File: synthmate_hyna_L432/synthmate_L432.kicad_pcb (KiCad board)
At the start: 4 copper layers, 74 x 23 mm, 43 parts, among them J1 USB_C_synthmate, J3 USB_C_connector_board, J5 Conn_01x15, J7 Conn_01x04, J8 Conn_ST_STDC14, SW1 RotaryEncoder_Switch, SW2 SW_Push, SW3 SW_Push, U1 STM32L432KCUx, U2 TS3USB221ARSER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

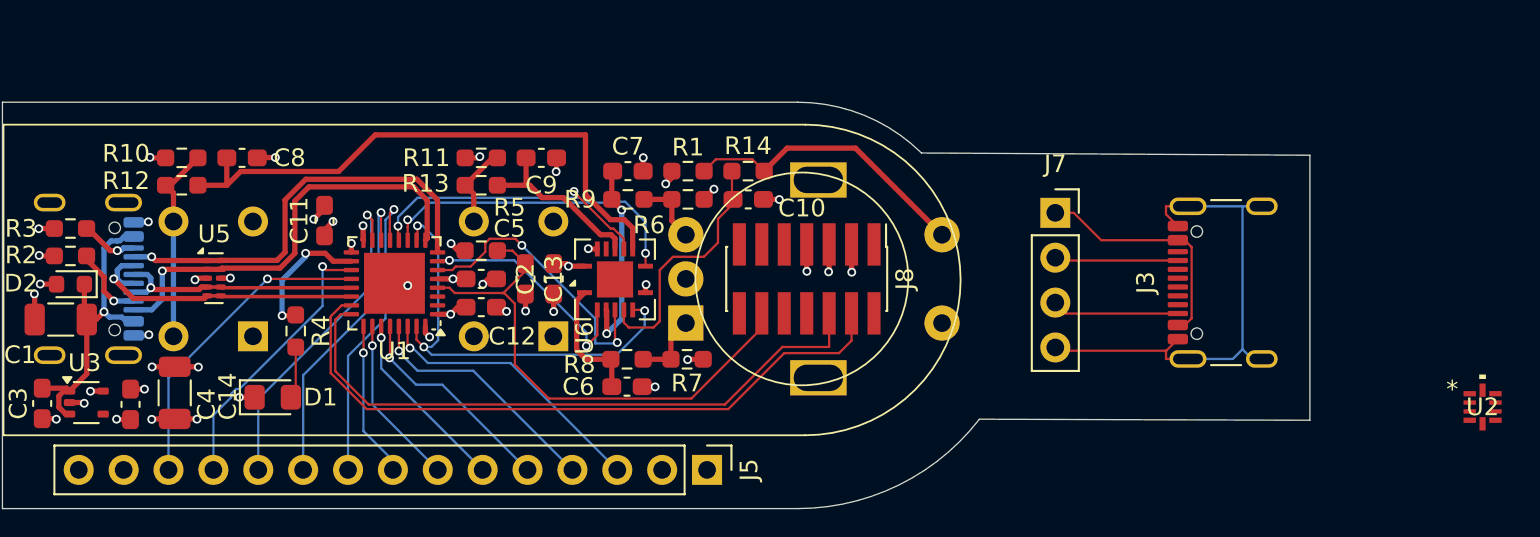
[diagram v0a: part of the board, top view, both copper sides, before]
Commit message: adapter board cleanup, uart IO protection added
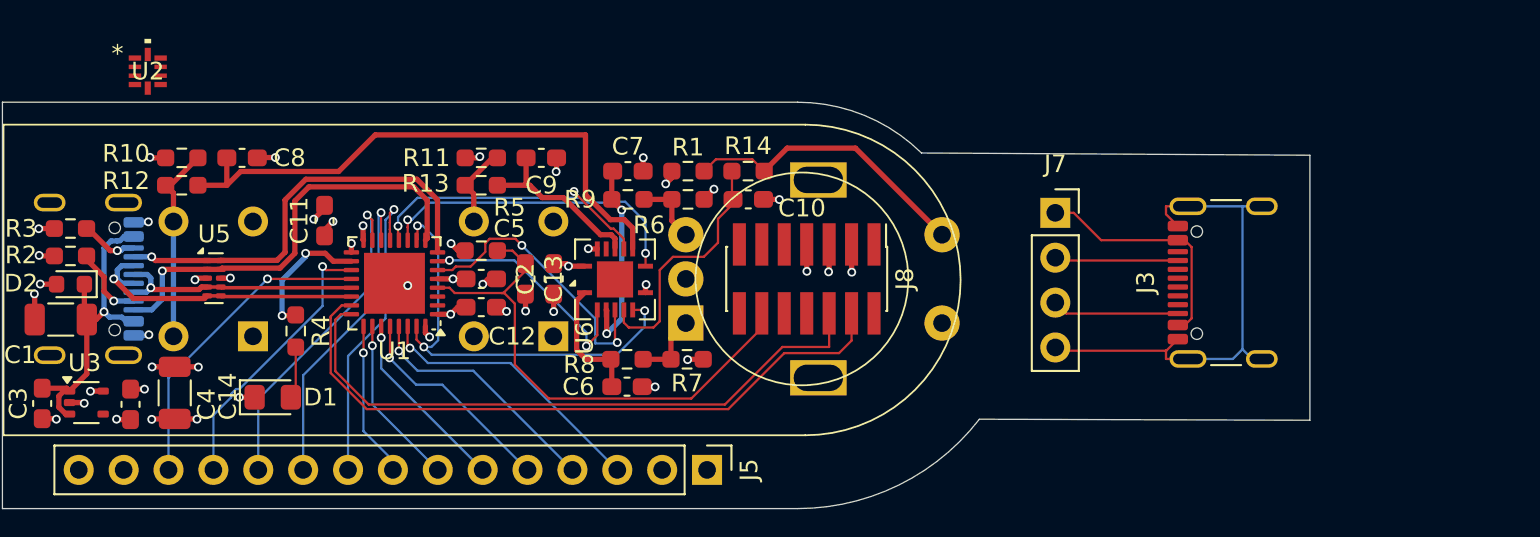
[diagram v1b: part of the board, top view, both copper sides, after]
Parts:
- moved U2 77.9 mm to (99.2, 35.2)
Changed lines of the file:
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@@
 	(footprint "footprints:RSE10"
 		(layer "F.Cu")
-		(at 174.7726 54.249999)
+		(at 99.2274 35.25)
 		(tags "TS3USB221ARSER ")
 		(property "Reference" "U2"

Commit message: V2_gerber
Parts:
- removed J3: USB_C_connector_board, Connector_USB:USB_C_Receptacle_GCT_USB4105-xx-A_16P_TopMnt_Horizontal
- removed J5: Conn_01x15, Connector_PinHeader_2.54mm:PinHeader_1x15_P2.54mm_Vertical
- removed J7: Conn_01x04, Connector_PinSocket_2.54mm:PinSocket_1x04_P2.54mm_Vertical
- removed U5: TPD4E02B04DQA, Package_SON:USON-10_2.5x1.0mm_P0.5mm
- added C15: 1uF, Capacitor_SMD:C_0603_1608Metric_Pad1.08x0.95mm_HandSolder, F.Cu at (104.0, 51.3)
- added C16: 1uF, Capacitor_SMD:C_0603_1608Metric_Pad1.08x0.95mm_HandSolder, F.Cu at (98.1, 40.7)
- added D3: D_Schottky, Diode_SMD:D_0603_1608Metric, F.Cu at (110.8, 42.0)
- added H1: MountingHole, MountingHole:MountingHole_2.1mm, F.Cu at (94.1, 39.3)
- added H2: MountingHole, MountingHole:MountingHole_2.1mm, F.Cu at (124.8, 53.5)
- added R16: 220R, Resistor_SMD:R_0603_1608Metric_Pad0.98x0.95mm_HandSolder, F.Cu at (104.5, 44.1)
- added R18: 20k, Resistor_SMD:R_0603_1608Metric_Pad0.98x0.95mm_HandSolder, F.Cu at (102.9, 53.7)
- added TP1: TestPoint, TestPoint:TestPoint_Pad_1.0x1.0mm, F.Cu at (107.0, 39.3)
- added TP2: TestPoint, TestPoint:TestPoint_Pad_1.0x1.0mm, F.Cu at (108.5, 54.9)
- added TP3: TestPoint, TestPoint:TestPoint_Pad_1.0x1.0mm, F.Cu at (110.6, 54.9)
- added TP4: TestPoint, TestPoint:TestPoint_Pad_1.0x1.0mm, F.Cu at (109.1, 39.3)
- added TP5: TestPoint, TestPoint:TestPoint_Pad_1.0x1.0mm, F.Cu at (123.5, 39.8)
- added TP6: TestPoint, TestPoint:TestPoint_Pad_1.0x1.0mm, F.Cu at (124.4, 49.6)
- added U4: SN74LV1T34DBV, Package_TO_SOT_SMD:SOT-23-5, F.Cu at (101.7, 43.7)
- C10, C11, C12, C2, C5, C6, C7, C8, C9: value 100nF -> 1uF
- J1: moved to F.Cu
- SW2, SW3: footprint Button_Switch_THT:SW_TH_Tactile_Omron_B3F-10xx -> Button_Switch_THT:Marquardt_6450
- moved U2 14.3 mm to (103.4, 49.0), turned to 180 degrees
- moved U6 10.6 mm to (117.1, 53.2), turned to 0 degrees
- moved C6 7.84 mm to (125.8, 45.3), turned to -90 degrees
- moved R8 6.34 mm to (127.3, 45.3), turned to -90 degrees
- moved SW2 5.45 mm to (100.8, 47.0), turned to 0 degrees
- moved SW3 5.43 mm to (117.8, 47.0), turned to 0 degrees
- moved C13 4.07 mm to (120.4, 50.6), turned to 90 degrees
- moved C2 3.89 mm to (122.0, 50.6), turned to 90 degrees
- moved R5 3.25 mm to (116.9, 42.4)
- moved R10 3.23 mm to (98.1, 39.1)
- moved C5 3.16 mm to (116.9, 44.1)
- moved C8 3.06 mm to (101.7, 39.1)
- moved R7 2.19 mm to (127.7, 50.9), turned to -90 degrees
- moved C9 1.54 mm to (120.3, 39.2)
- moved R11 1.54 mm to (116.9, 39.2)
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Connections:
- J1 pad A6: USB_DP -> /usb_P
- J1 pad A7: USB_DN -> /usb_N
- J1 pad A8: LPUART_TX -> unconnected-(J1-SBU1-PadA8)
- J1 pad B6: USB_DP -> /usb_P
- J1 pad B7: USB_DN -> /usb_N
- J1 pad B8: LPUART_RX -> unconnected-(J1-SBU2-PadB8)
- SW3 pad 1: GND -> Net-(R11-Pad1)
- SW3 pad 2: Net-(R11-Pad1) -> GND
- U1 pad 13: PA7 -> usb_switch
- U1 pad 19: USART1_TX -> Net-(U1-PA9)
- U1 pad 21: USB_DN -> /usb_mcu_N
- U1 pad 22: USB_DP -> /usb_mcu_P
- U1 pad 25: PA15 -> Net-(U1-PA15)
- U2 pad 1: unconnected-(U2-1D+-Pad1) -> USART1_TX
- U2 pad 10: unconnected-(U2-VCC-Pad10) -> 3V3
- U2 pad 2: unconnected-(U2-1D--Pad2) -> USART1_RX
- U2 pad 3: unconnected-(U2-2D+-Pad3) -> /usb_mcu_P
- U2 pad 4: unconnected-(U2-2D--Pad4) -> /usb_mcu_N
- U2 pad 5: unconnected-(U2-GND-Pad5) -> GND
- U2 pad 6: unconnected-(U2-*OE-Pad6) -> GND
- U2 pad 7: unconnected-(U2-D--Pad7) -> /usb_N
- U2 pad 8: unconnected-(U2-D+-Pad8) -> /usb_P
- U2 pad 9: unconnected-(U2-S-Pad9) -> usb_switch
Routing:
- net adaptor_GND: track 28.5 -> 0.00 mm
- net usb_switch: track 0.00 -> 24.6 mm, vias 0 -> 3
- net GND: track 27.6 -> 49.2 mm, vias 31 -> 26
- net PB1: track 18.7 -> 0.00 mm, vias 1 -> 0
- net Net-(C10-Pad1): track 14.2 -> 32.5 mm, vias 0 -> 2
- net PB0: track 18.0 -> 0.00 mm, vias 1 -> 0
- net PA7: track 17.7 -> 0.00 mm, vias 1 -> 0
- net Net-(U1-PA9): track 0.00 -> 17.2 mm, vias 0 -> 2
- net USB_DP: track 17.1 -> 0.00 mm, vias 1 -> 0
- net PB7: track 15.9 -> 0.00 mm, vias 1 -> 0
- net 3V3: track 18.7 -> 34.5 mm, vias 16 -> 17
- net USB_DN: track 14.1 -> 0.00 mm, vias 1 -> 0
- net PB6: track 14.0 -> 0.00 mm, vias 1 -> 0
- net adaptor_5V: track 13.5 -> 0.00 mm
- net PB5: track 12.3 -> 0.00 mm, vias 1 -> 0
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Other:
- board size 74 x 23 mm -> 55 x 20 mm
- board text removed: "3V3 GND PB7 PB6 PB5 PB4 PB3 PA15 PA7 PB0 PB1 USART_TX USART_RX GND 3V3"

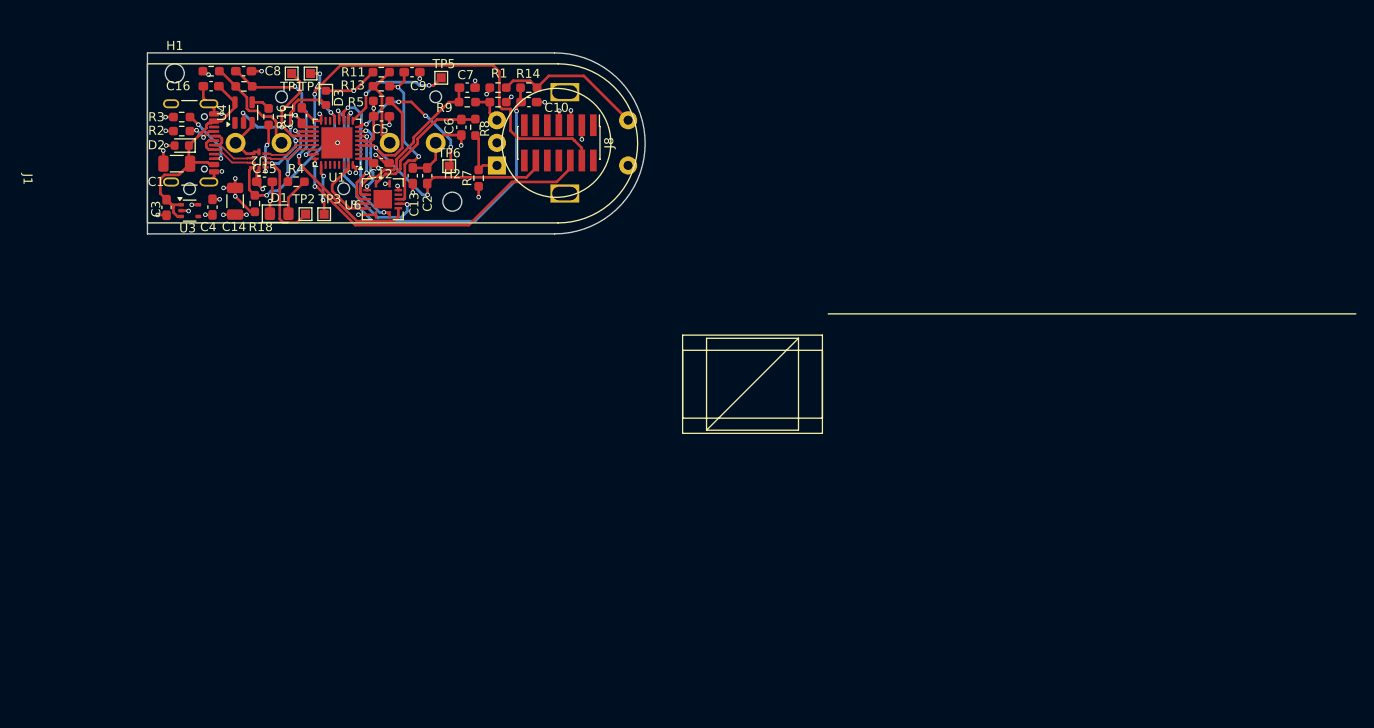
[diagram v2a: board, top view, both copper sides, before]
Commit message: before autorouter, locked footprints and usb
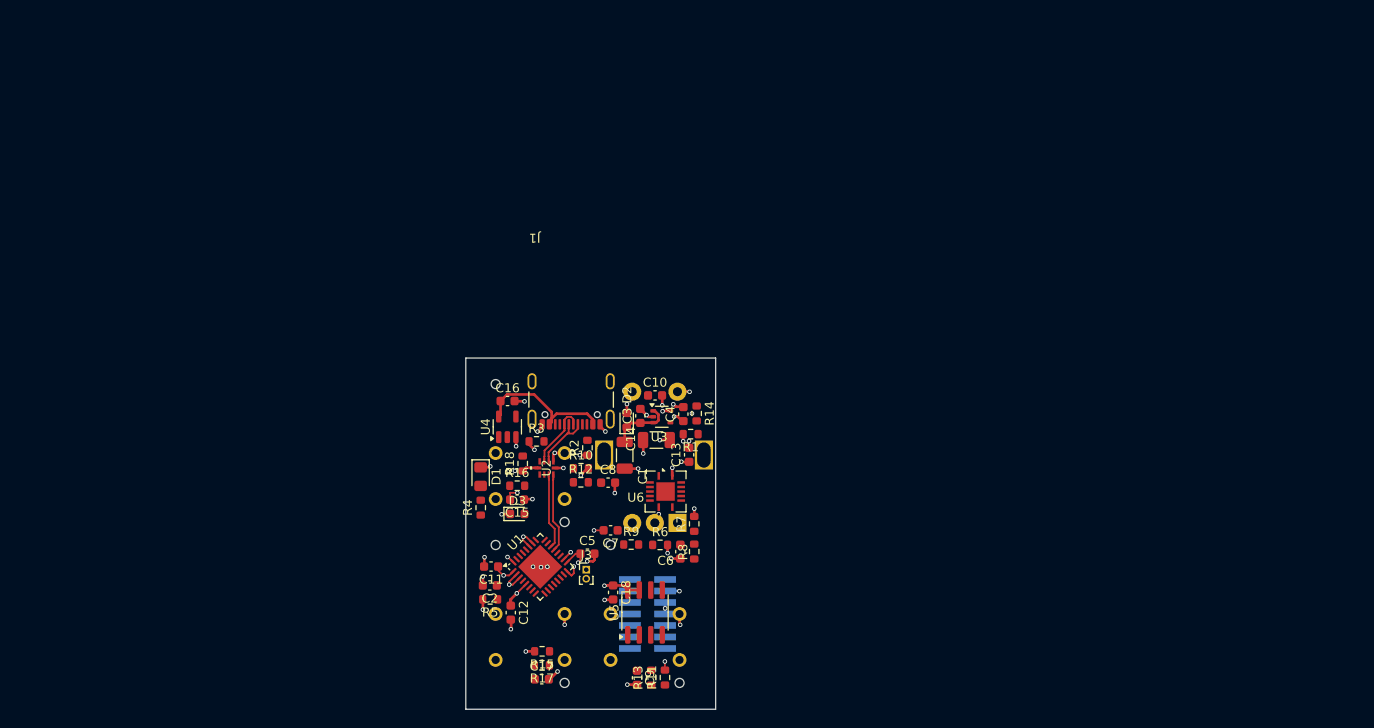
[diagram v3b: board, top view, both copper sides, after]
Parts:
- removed H1, H2: MountingHole, MountingHole:MountingHole_2.1mm
- removed TP1, TP2, TP3, TP4, TP5, TP6: TestPoint, TestPoint:TestPoint_Pad_1.0x1.0mm
- added C17: 1uF, Capacitor_SMD:C_0603_1608Metric, F.Cu at (134.6, 106.3)
- added C18: 1uF, Capacitor_SMD:C_0603_1608Metric, F.Cu at (142.5, 96.7)
- added J3: Conn_01x02, Connector_PinHeader_1.00mm:PinHeader_1x02_P1.00mm_Vertical, F.Cu at (139.6, 94.2)
- added R15: 10k, Resistor_SMD:R_0603_1608Metric, F.Cu at (134.7, 103.2)
- added R17: 10k, Resistor_SMD:R_0603_1608Metric, F.Cu at (134.7, 104.7)
- added SW5: PB_86_A1, PB86:PB_86_A0, B.Cu at (133.3, 81.3)
- added U5: M95256-WMN6P, Package_SO:SOIC-8_3.9x4.9mm_P1.27mm, F.Cu at (146.0, 98.9)
- C10, C11, C12, C13, C15, C16, C2, C3, C4, C5, C6, C7, C8, C9: footprint Capacitor_SMD:C_0603_1608Metric_Pad1.08x0.95mm_HandSolder -> Capacitor_SMD:C_0603_1608Metric
- J8: moved to B.Cu
- R1, R10, R11, R12, R13, R14, R16, R18, R2, R3, R4, R5, R6, R7, R8, R9: footprint Resistor_SMD:R_0603_1608Metric_Pad0.98x0.95mm_HandSolder -> Resistor_SMD:R_0603_1608Metric
- SW2, SW3: value SW_Push -> PB_86_A1; footprint Button_Switch_THT:Marquardt_6450 -> PB86:PB_86_A0
- U3: value MIC5365-1.0YC5 -> MIC5365-3.3YC5
- moved R11 73.9 mm to (148.2, 106.1), turned to 90 degrees
- moved R13 71.9 mm to (146.7, 106.1), turned to 90 degrees
- moved C9 71.4 mm to (145.2, 106.1), turned to -90 degrees
- moved SW2 69.0 mm to (146.1, 99.1), turned to 180 degrees
- moved C8 60.7 mm to (142.0, 84.5)
- moved R10 60.0 mm to (139.0, 83.0), turned to 0 degrees
- moved C1 59.1 mm to (143.8, 81.5), turned to -90 degrees
- moved D2 57.8 mm to (144.0, 77.7), turned to 90 degrees
- moved R12 57.4 mm to (139.0, 84.5)
- moved C3 57.2 mm to (145.5, 77.2), turned to 90 degrees
- moved U3 56.9 mm to (147.9, 77.3)
- moved R2 56.9 mm to (139.7, 80.7), turned to 90 degrees
- moved C4 56.8 mm to (150.3, 77.0), turned to 90 degrees
- moved R5 56.4 mm to (128.9, 97.5)
- moved SW3 54.3 mm to (133.3, 99.1), turned to 180 degrees
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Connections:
- R10 pad 1: Net-(R10-Pad1) -> Net-(SW5-C)
- R11 pad 1: Net-(R11-Pad1) -> Net-(SW2-C)
- R12 pad 1: Net-(R10-Pad1) -> Net-(SW5-C)
- R13 pad 1: Net-(R11-Pad1) -> Net-(SW2-C)
- SW2 pad 2: Net-(R10-Pad1) -> Net-(SW2-C)
- SW3 pad 1: Net-(R11-Pad1) -> GND
- SW3 pad 2: GND -> Net-(SW3-C)
- U1 pad 10: BOOT0 -> CS
- U1 pad 11: pushbutton_A -> SCK
- U1 pad 12: pushbutton_B -> MISO
- U1 pad 13: usb_switch -> MOSI
- U1 pad 14: PB0 -> Net-(J3-Pin_2)
- U1 pad 15: PB1 -> Net-(J3-Pin_1)
- U1 pad 18: LED -> GND
- U1 pad 2: unconnected-(U1-PC14-Pad2) -> GND
- U1 pad 25: Net-(U1-PA15) -> LED
- U1 pad 26: PB3 -> GND
- U1 pad 27: PB4 -> GND
- U1 pad 28: PB5 -> pushbutton_A
- U1 pad 29: PB6 -> pushbutton_B
- U1 pad 3: unconnected-(U1-PC15-Pad3) -> GND
- U1 pad 30: PB7 -> pushbutton_C
- U1 pad 8: LPUART_TX -> BOOT0
- U1 pad 9: LPUART_RX -> usb_switch
- U6 pad 12: unconnected-(U6-Pad12) -> pushbutton_A
- U6 pad 13: GND -> Net-(C17-Pad1)
- U6 pad 8: pushbutton_A -> pushbutton_C
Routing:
- net SWDIO: track 47.9 -> 0.00 mm, vias 2 -> 0
- net SWCLK: track 35.7 -> 0.00 mm, vias 2 -> 0
- net NRST: track 33.1 -> 0.00 mm, vias 2 -> 0
- net Net-(C10-Pad1): track 32.5 -> 0.00 mm, vias 2 -> 0
- net Net-(C8-Pad1): track 31.3 -> 0.00 mm, vias 2 -> 0
- net USART1_RX: track 25.2 -> 0.00 mm, vias 3 -> 0
- net usb_switch: track 24.6 -> 0.00 mm, vias 3 -> 0
- net pushbutton_B: track 20.1 -> 0.00 mm, vias 2 -> 0
- net Net-(C7-Pad1): track 18.7 -> 0.00 mm
- net Net-(C9-Pad1): track 17.9 -> 0.00 mm, vias 2 -> 0
- net Net-(U1-PA9): track 17.2 -> 0.00 mm, vias 2 -> 0
- net BOOT0: track 17.0 -> 0.00 mm, vias 2 -> 0
- net Net-(R1-Pad1): track 16.7 -> 0.00 mm, vias 0 -> 1
- net pushbutton_A: track 16.4 -> 0.00 mm, vias 2 -> 0
- net LPUART_TX: track 16.0 -> 0.00 mm, vias 4 -> 0
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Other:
- board size 55 x 20 mm -> 27.6 x 38.8 mm

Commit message: naming cleanup
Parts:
- D2, D3: value D_Schottky -> 1N5819WS; footprint Diode_SMD:D_0603_1608Metric -> Diode_SMD:D_SOD-323
- J1: value USB_C_synthmate -> USB4105-GF-A-120
- U1: value STM32L432KCUx -> STM32L432KBU6
- U4: value SN74LV1T34DBV -> SN74LV1T34DBVR
- U5: value M95256-WMN6P -> M95M04-DRMN6TP
- U6: value 74LV14 -> SN74LV14APWR; footprint Package_DFN_QFN:Texas_S-PVQFN-N14 -> Package_SO:TSSOP-14_4.4x5mm_P0.65mm
- moved C13 25.7 mm to (139.6, 104.5), turned to 0 degrees
- moved U6 23.3 mm to (133.3, 103.3), turned to -90 degrees
- moved D1 21.2 mm to (149.0, 85.5), turned to 180 degrees
- moved R4 17.8 mm to (145.6, 85.6), turned to 0 degrees
- moved R15 5.34 mm to (139.7, 101.5)
- moved R17 5.34 mm to (139.7, 103.0), turned to 0 degrees
- moved C17 5.04 mm to (139.7, 106.0)
- moved R5 4.25 mm to (129.7, 101.6), turned to -90 degrees
- moved R1 3.94 mm to (150.4, 83.1), turned to -90 degrees
- moved C1 3.55 mm to (147.0, 83.0), turned to 0 degrees
- moved R14 3.43 mm to (150.4, 80.1)
- moved C12 1.00 mm to (131.4, 97.9)
- moved C2 0.91 mm to (129.5, 96.6), turned to -90 degrees
- moved U2 0.91 mm to (135.2, 83.8)
- moved C11 0.52 mm to (129.5, 93.6), turned to 90 degrees
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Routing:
- net GND: track 46.8 -> 109.6 mm, vias 40 -> 80
- net Net-(C8-Pad1): track 0.00 -> 45.7 mm, vias 0 -> 2
- net Net-(C10-Pad1): track 0.00 -> 43.0 mm, vias 0 -> 2
- net 5V: track 23.2 -> 65.9 mm
- net NRST: track 0.00 -> 35.0 mm, vias 0 -> 1
- net usb_switch: track 0.00 -> 34.3 mm, vias 0 -> 4
- net 3V3: track 32.4 -> 60.0 mm, vias 20 -> 45
- net pushbutton_A: track 0.00 -> 26.4 mm, vias 0 -> 2
- net Net-(C6-Pad1): track 0.00 -> 25.8 mm
- net pushbutton_B: track 0.00 -> 22.3 mm, vias 0 -> 2
- net pushbutton_C: track 0.00 -> 21.7 mm
- net SWCLK: track 0.00 -> 20.8 mm, vias 0 -> 1
- net SWDIO: track 0.00 -> 20.7 mm, vias 0 -> 1
- net Net-(U1-PA9): track 0.00 -> 18.7 mm, vias 0 -> 2
- net Net-(C7-Pad1): track 0.00 -> 17.3 mm, vias 0 -> 2
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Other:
- board size 27.6 x 38.8 mm -> 28.1 x 38.8 mm

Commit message: 23_1
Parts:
- added J5: Conn_01x04, Connector_PinHeader_2.54mm:PinHeader_1x04_P2.54mm_Vertical, F.Cu at (151.6, 105.6)
- U3: value MIC5365-3.3YC5 -> MIC5365-3.3YC5-TR
- moved R5 12.5 mm to (130.2, 89.1), turned to 90 degrees
- moved D1 8.36 mm to (149.6, 77.2), turned to 0 degrees
- moved R1 8.36 mm to (144.0, 77.7)
- moved R4 7.53 mm to (149.2, 78.9)
- moved U3 7.19 mm to (146.7, 84.3), turned to -90 degrees
- moved R7 6.69 mm to (149.8, 95.6), turned to -90 degrees
- moved R14 5.48 mm to (145.4, 77.7), turned to 90 degrees
- moved C14 5.20 mm to (149.3, 84.6), turned to -90 degrees
- moved C4 4.72 mm to (149.0, 81.5), turned to 180 degrees
- moved C9 4.64 mm to (140.5, 106.1), turned to 180 degrees
- moved D2 4.18 mm to (146.5, 81.0)
- moved C3 3.87 mm to (143.9, 80.7)
- moved R15 3.72 mm to (139.9, 97.7), turned to 90 degrees
- moved C1 3.33 mm to (144.1, 84.5), turned to -90 degrees
- moved C13 3.23 mm to (137.7, 102.0)
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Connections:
- U5 pad 3: GND -> 3V3
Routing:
- net GND: track 109.6 -> 59.6 mm, vias 80 -> 45
- net 5V: track 65.9 -> 30.2 mm
- net 3V3: track 60.0 -> 29.4 mm, vias 45 -> 24
- net usb_switch: track 34.3 -> 21.2 mm, vias 4 -> 2
- net Net-(R1-Pad1): track 17.1 -> 4.26 mm
- net LED: track 14.0 -> 23.7 mm
- net SWDIO: track 20.7 -> 30.2 mm
- net NRST: track 35.0 -> 26.9 mm
- net /usb_N: track 15.8 -> 7.77 mm
- net /usb_P: track 16.3 -> 8.40 mm
- net /usb_mcu_N: track 15.4 -> 7.90 mm
- net Net-(C7-Pad1): track 17.3 -> 24.7 mm
- net /usb_mcu_P: track 15.0 -> 7.60 mm
- net enc_B: track 4.64 -> 11.4 mm
- net Net-(C8-Pad1): track 45.7 -> 39.6 mm
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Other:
- board size 28.1 x 38.8 mm -> 28 x 38 mm
- board text added: "3V3 SWDIO SWCLK GND"
